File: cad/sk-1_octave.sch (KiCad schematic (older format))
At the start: 16 parts, among them U1 4069, U2 74HC74, U3 74LS157

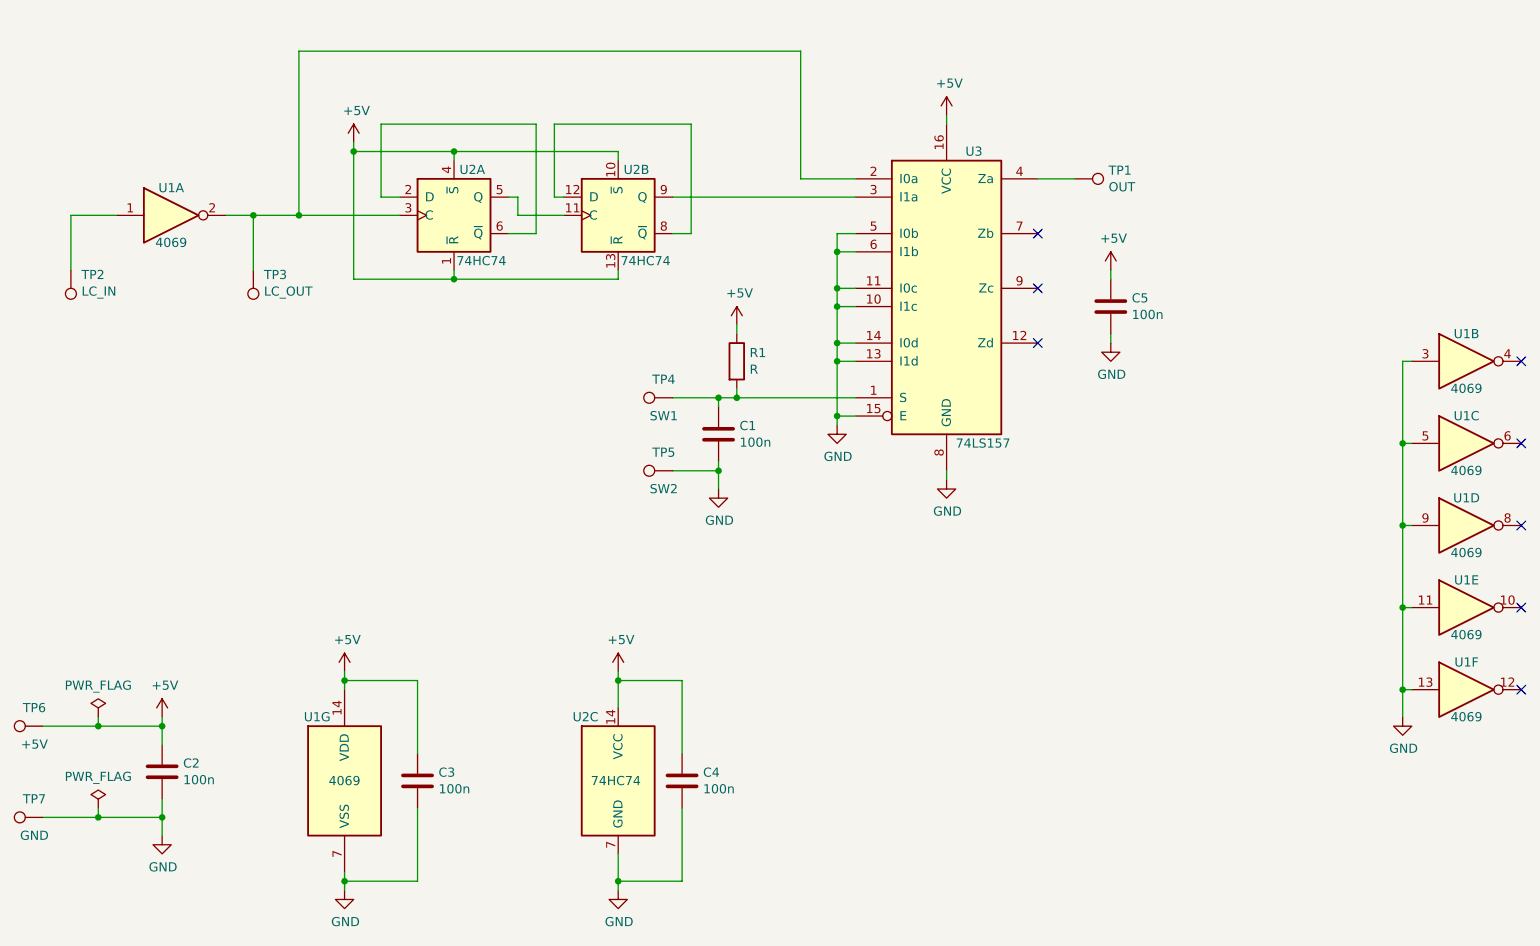
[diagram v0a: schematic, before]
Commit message: Added output signal conditioning.
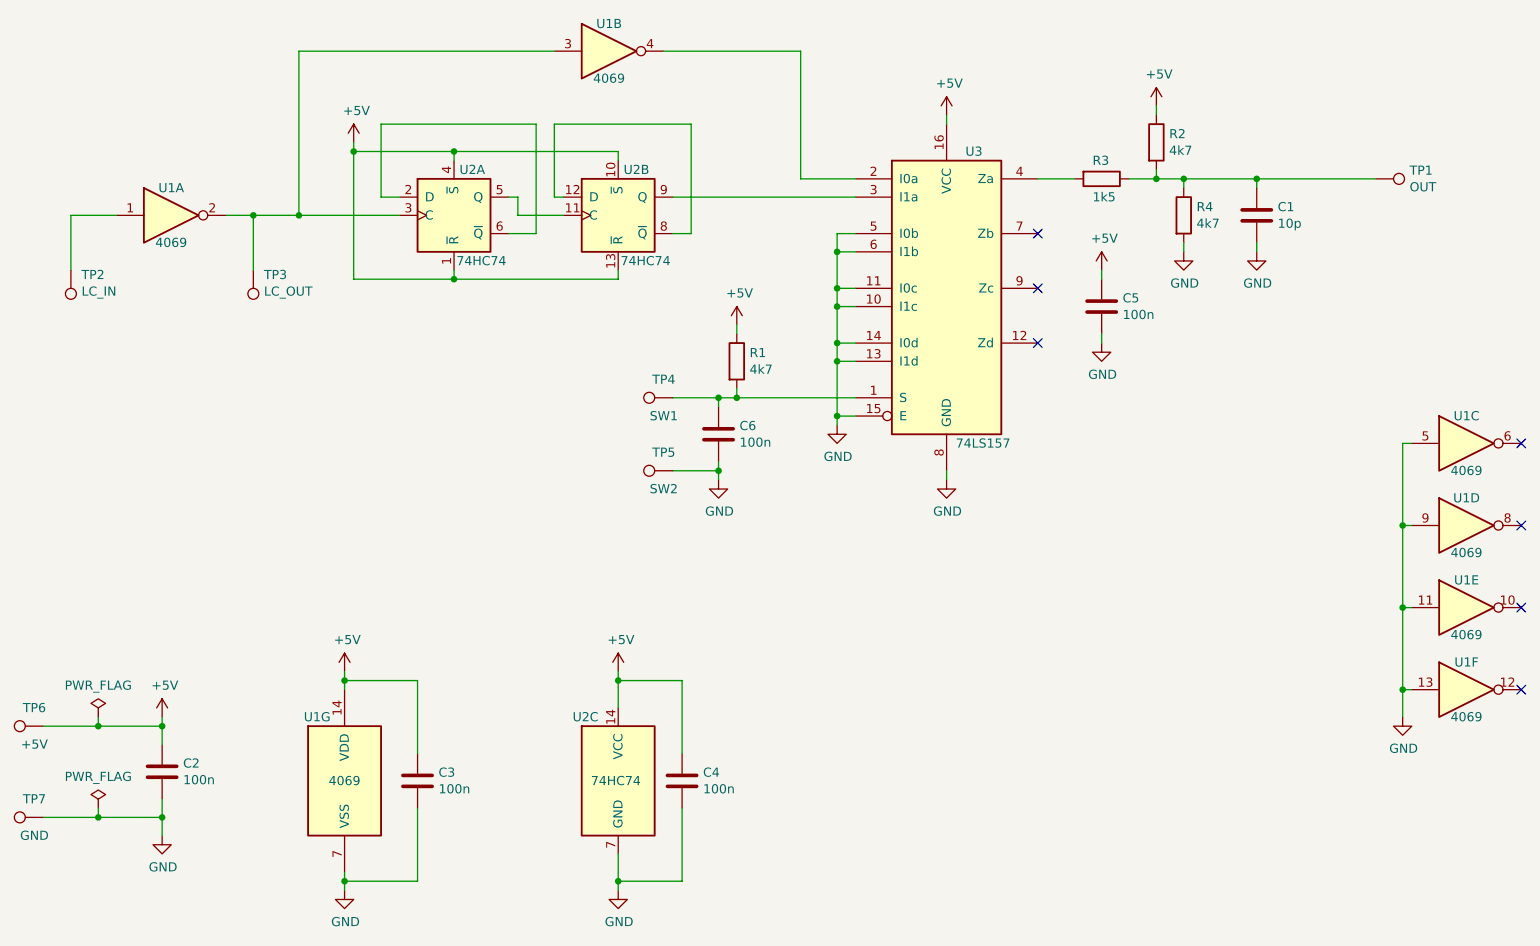
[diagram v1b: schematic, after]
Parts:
- added C6: 100n, Capacitor_SMD:C_0603_1608Metric_Pad1.08x0.95mm_HandSolder, symbol Device:C
- added R2, R4: 4k7, Resistor_SMD:R_0603_1608Metric_Pad0.98x0.95mm_HandSolder, symbol Device:R
- added R3: 1k5, Resistor_SMD:R_0603_1608Metric_Pad0.98x0.95mm_HandSolder, symbol Device:R
- C1: value 100n -> 10p
- R1: value R -> 4k7
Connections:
- net +5V: now also R2.1
- net GND: now also C6.2, R4.2; no longer U1.3
- net at TP3.1, U1.2, U2.3 (C): now also U1.3; no longer U3.2 (I0a)
- net at U1.4: now also U3.2 (I0a)
- net at R1.2, TP4.1, U3.1 (S): now also C6.1; no longer C1.1
- net at U3.4 (Za): now also R3.2; no longer TP1.1
- new net: C1.1, R2.2, R3.1, R4.1, TP1.1
- no-connect marks 8 -> 7
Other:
- moved on the sheet: C1, C5, TP1, U1B
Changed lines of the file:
@@
 	9300 5950 9300 5800
 Wire Wire Line
-	9300 4000 9350 4000
-Wire Wire Line
 	9350 4450 9300 4450
-Connection ~ 9300 4450
-Wire Wire Line
-	9300 4450 9300 4000
 Wire Wire Line
 	9350 4900 9300 4900
@@
 Wire Wire Line
 	9300 5800 9300 5350
-NoConn ~ 9950 4000
 NoConn ~ 9950 4450
 NoConn ~ 9950 4900
@@
 L 4xxx:4069 U1
 U 2 1 604A98CC
-P 9650 4000
-F 0 "U1" H 9650 4150 50  0000 C CNN
-F 1 "4069" H 9650 3850 50  0000 C CNN
-F 2 "Package_SO:SO-14_3.9x8.65mm_P1.27mm" H 9650 4000 50  0001 C CNN
-F 3 "" H 9650 4000 50  0001 C CNN
-F 4 "CD4069UBM" H 9650 4000 50  0001 C CNN "pn"
-	2    9650 4000
+P 4950 2300
+F 0 "U1" H 4950 2450 50  0000 C CNN
+F 1 "4069" H 4950 2150 50  0000 C CNN
+F 2 "Package_SO:SO-14_3.9x8.65mm_P1.27mm" H 4950 2300 50  0001 C CNN
+F 3 "" H 4950 2300 50  0001 C CNN
+F 4 "CD4069UBM" H 4950 2300 50  0001 C CNN "pn"
+	2    4950 2300
 	1    0    0    -1
 $EndComp
@@
 	3250 3200 3250 2300
 Wire Wire Line
-	3250 2300 6000 2300
+	3250 2300 4650 2300
 Wire Wire Line
 	6000 2300 6000 3000
@@
 L Connector:TestPoint TP1
 U 1 1 604F8CEF
-P 7500 3000
-F 0 "TP1" V 7454 3188 50  0000 L CNN
-F 1 "OUT" V 7545 3188 50  0000 L CNN
-F 2 "TestPoint:TestPoint_Pad_D2.0mm" H 7700 3000 50  0001 C CNN
-F 3 "~" H 7700 3000 50  0001 C CNN
-	1    7500 3000
+P 9150 3000
+F 0 "TP1" V 9104 3188 50  0000 L CNN
+F 1 "OUT" V 9195 3188 50  0000 L CNN
+F 2 "TestPoint:TestPoint_Pad_D2.0mm" H 9350 3000 50  0001 C CNN
+F 3 "~" H 9350 3000 50  0001 C CNN
+	1    9150 3000
 	0    1    1    0
 $EndComp
@@
 	0    -1   -1   0
 $EndComp
-$Comp
-L power:GND #PWR06
-U 1 1 605025E7
-P 5550 4700
-F 0 "#PWR06" H 5550 4450 50  0001 C CNN
-F 1 "GND" H 5555 4527 50  0000 C CNN
-F 2 "" H 5550 4700 50  0001 C CNN
-F 3 "" H 5550 4700 50  0001 C CNN
-	1    5550 4700
-	1    0    0    -1
-$EndComp
-Wire Wire Line
-	5550 4700 5550 4600
 Wire Wire Line
 	6300 4200 5650 4200
@@
 P 5650 4000
 F 0 "R1" H 5720 4046 50  0000 L CNN
-F 1 "R" H 5720 3955 50  0000 L CNN
+F 1 "4k7" H 5720 3955 50  0000 L CNN
 F 2 "Resistor_SMD:R_0603_1608Metric_Pad0.98x0.95mm_HandSolder" V 5580 4000 50  0001 C CNN
 F 3 "~" H 5650 4000 50  0001 C CNN
@@
 Wire Wire Line
 	5650 4150 5650 4200
-$Comp
-L Device:C C1
-U 1 1 60519FBF
-P 5550 4400
-F 0 "C1" H 5665 4446 50  0000 L CNN
-F 1 "100n" H 5665 4355 50  0000 L CNN
-F 2 "Capacitor_SMD:C_0603_1608Metric_Pad1.08x0.95mm_HandSolder" H 5588 4250 50  0001 C CNN
-F 3 "~" H 5550 4400 50  0001 C CNN
-	1    5550 4400
-	1    0    0    -1
-$EndComp
-Wire Wire Line
-	5550 4600 5550 4550
 Wire Wire Line
 	5550 4250 5550 4200
@@
 Wire Wire Line
 	5550 4200 5300 4200
-Connection ~ 5550 4600
-Wire Wire Line
-	5300 4600 5550 4600
 $Comp
 L Connector:TestPoint TP6
@@
 L Device:C C5
 U 1 1 60582340
-P 7700 3700
-F 0 "C5" H 7815 3746 50  0000 L CNN
-F 1 "100n" H 7815 3655 50  0000 L CNN
-F 2 "Capacitor_SMD:C_0603_1608Metric_Pad1.08x0.95mm_HandSolder" H 7738 3550 50  0001 C CNN
-F 3 "~" H 7700 3700 50  0001 C CNN
-	1    7700 3700
+P 7650 3700
+F 0 "C5" H 7765 3746 50  0000 L CNN
+F 1 "100n" H 7765 3655 50  0000 L CNN
+F 2 "Capacitor_SMD:C_0603_1608Metric_Pad1.08x0.95mm_HandSolder" H 7688 3550 50  0001 C CNN
+F 3 "~" H 7650 3700 50  0001 C CNN
+	1    7650 3700
 	1    0    0    -1
 $EndComp
@@
 L power:+5V #PWR014
 U 1 1 60582B8C
-P 7700 3500
-F 0 "#PWR014" H 7700 3350 50  0001 C CNN
-F 1 "+5V" H 7715 3673 50  0000 C CNN
-F 2 "" H 7700 3500 50  0001 C CNN
-F 3 "" H 7700 3500 50  0001 C CNN
-	1    7700 3500
+P 7650 3500
+F 0 "#PWR014" H 7650 3350 50  0001 C CNN
+F 1 "+5V" H 7665 3673 50  0000 C CNN
+F 2 "" H 7650 3500 50  0001 C CNN
+F 3 "" H 7650 3500 50  0001 C CNN
+	1    7650 3500
 	1    0    0    -1
 $EndComp
@@
 L power:GND #PWR015
 U 1 1 6058572C
-P 7700 3900
-F 0 "#PWR015" H 7700 3650 50  0001 C CNN
-F 1 "GND" H 7705 3727 50  0000 C CNN
-F 2 "" H 7700 3900 50  0001 C CNN
-F 3 "" H 7700 3900 50  0001 C CNN
-	1    7700 3900
-	1    0    0    -1
-$EndComp
-Wire Wire Line
-	7700 3900 7700 3850
-Wire Wire Line
-	7700 3550 7700 3500
+P 7650 3900
+F 0 "#PWR015" H 7650 3650 50  0001 C CNN
+F 1 "GND" H 7655 3727 50  0000 C CNN
+F 2 "" H 7650 3900 50  0001 C CNN
+F 3 "" H 7650 3900 50  0001 C CNN
+	1    7650 3900
+	1    0    0    -1
+$EndComp
+Wire Wire Line
+	7650 3900 7650 3850
+Wire Wire Line
+	7650 3550 7650 3500
+Wire Wire Line
+	5250 2300 6000 2300
+$Comp
+L power:+5V #PWR016
+U 1 1 604EF03E
+P 7950 2600
+F 0 "#PWR016" H 7950 2450 50  0001 C CNN
+F 1 "+5V" H 7965 2773 50  0000 C CNN
+F 2 "" H 7950 2600 50  0001 C CNN
+F 3 "" H 7950 2600 50  0001 C CNN
+	1    7950 2600
+	1    0    0    -1
+$EndComp
+$Comp
+L Device:R R2
+U 1 1 604EF044
+P 7950 2800
+F 0 "R2" H 8020 2846 50  0000 L CNN
+F 1 "4k7" H 8020 2755 50  0000 L CNN
+F 2 "Resistor_SMD:R_0603_1608Metric_Pad0.98x0.95mm_HandSolder" V 7880 2800 50  0001 C CNN
+F 3 "~" H 7950 2800 50  0001 C CNN
+	1    7950 2800
+	1    0    0    -1
+$EndComp
+Wire Wire Line
+	7950 2600 7950 2650
+$Comp
+L Device:R R4
+U 1 1 604F1FC9
+P 8100 3200
+F 0 "R4" H 8170 3246 50  0000 L CNN
+F 1 "4k7" H 8170 3155 50  0000 L CNN
+F 2 "Resistor_SMD:R_0603_1608Metric_Pad0.98x0.95mm_HandSolder" V 8030 3200 50  0001 C CNN
+F 3 "~" H 8100 3200 50  0001 C CNN
+	1    8100 3200
+	1    0    0    -1
+$EndComp
+$Comp
+L Device:R R3
+U 1 1 604F8A19
+P 7650 3000
+F 0 "R3" V 7550 2950 50  0000 L CNN
+F 1 "1k5" V 7750 2950 50  0000 L CNN
+F 2 "Resistor_SMD:R_0603_1608Metric_Pad0.98x0.95mm_HandSolder" V 7580 3000 50  0001 C CNN
+F 3 "~" H 7650 3000 50  0001 C CNN
+	1    7650 3000
+	0    1    1    0
+$EndComp
+$Comp
+L Device:C C1
+U 1 1 60519FBF
+P 8500 3200
+F 0 "C1" H 8615 3246 50  0000 L CNN
+F 1 "10p" H 8615 3155 50  0000 L CNN
+F 2 "Capacitor_SMD:C_0603_1608Metric_Pad1.08x0.95mm_HandSolder" H 8538 3050 50  0001 C CNN
+F 3 "~" H 8500 3200 50  0001 C CNN
+	1    8500 3200
+	1    0    0    -1
+$EndComp
+Wire Wire Line
+	8500 3350 8500 3400
+$Comp
+L power:GND #PWR06
+U 1 1 605025E7
+P 8500 3400
+F 0 "#PWR06" H 8500 3150 50  0001 C CNN
+F 1 "GND" H 8505 3227 50  0000 C CNN
+F 2 "" H 8500 3400 50  0001 C CNN
+F 3 "" H 8500 3400 50  0001 C CNN
+	1    8500 3400
+	1    0    0    -1
+$EndComp
+Wire Wire Line
+	8100 3350 8100 3400
+$Comp
+L power:GND #PWR017
+U 1 1 6051DAC1
+P 8100 3400
+F 0 "#PWR017" H 8100 3150 50  0001 C CNN
+F 1 "GND" H 8105 3227 50  0000 C CNN
+F 2 "" H 8100 3400 50  0001 C CNN
+F 3 "" H 8100 3400 50  0001 C CNN
+	1    8100 3400
+	1    0    0    -1
+$EndComp
+Wire Wire Line
+	7800 3000 7950 3000
+Wire Wire Line
+	8100 3050 8100 3000
+Connection ~ 8100 3000
+Wire Wire Line
+	8100 3000 8500 3000
+Wire Wire Line
+	7950 2950 7950 3000
+Connection ~ 7950 3000
+Wire Wire Line
+	7950 3000 8100 3000
+Wire Wire Line
+	8500 3050 8500 3000
+Connection ~ 8500 3000
+Wire Wire Line
+	8500 3000 9150 3000
+$Comp
+L Device:C C6
+U 1 1 60532A4C
+P 5550 4400
+F 0 "C6" H 5665 4446 50  0000 L CNN
+F 1 "100n" H 5665 4355 50  0000 L CNN
+F 2 "Capacitor_SMD:C_0603_1608Metric_Pad1.08x0.95mm_HandSolder" H 5588 4250 50  0001 C CNN
+F 3 "~" H 5550 4400 50  0001 C CNN
+	1    5550 4400
+	1    0    0    -1
+$EndComp
+$Comp
+L power:GND #PWR018
+U 1 1 60532A52
+P 5550 4650
+F 0 "#PWR018" H 5550 4400 50  0001 C CNN
+F 1 "GND" H 5555 4477 50  0000 C CNN
+F 2 "" H 5550 4650 50  0001 C CNN
+F 3 "" H 5550 4650 50  0001 C CNN
+	1    5550 4650
+	1    0    0    -1
+$EndComp
+Wire Wire Line
+	5550 4650 5550 4600
+Wire Wire Line
+	5300 4600 5550 4600
+Connection ~ 5550 4600
+Wire Wire Line
+	5550 4600 5550 4550
 $EndSCHEMATC
